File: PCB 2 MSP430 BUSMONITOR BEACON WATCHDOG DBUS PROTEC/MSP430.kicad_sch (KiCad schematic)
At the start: 1 part

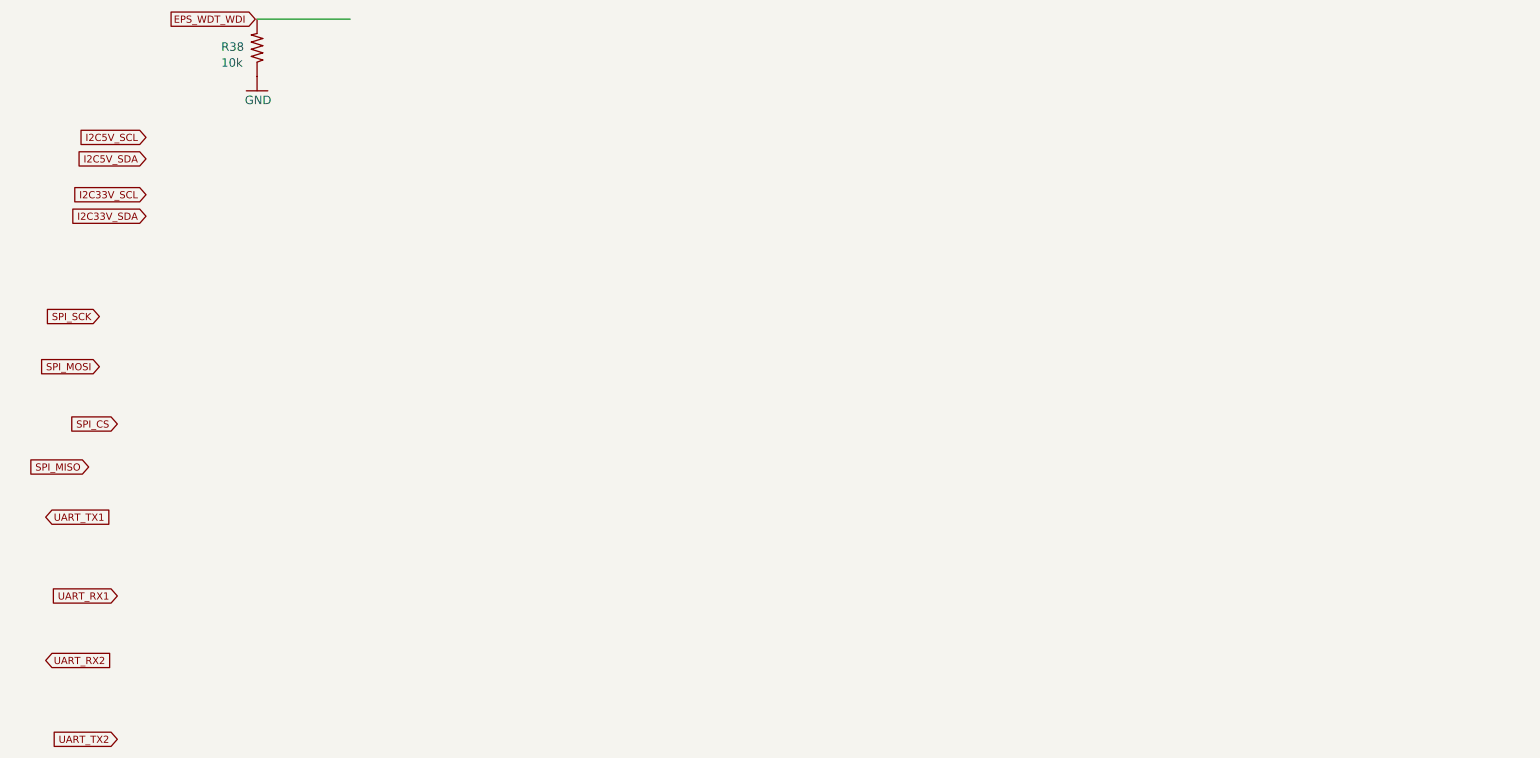
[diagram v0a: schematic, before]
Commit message: Changes
Added bucks from old work
and copied SPV
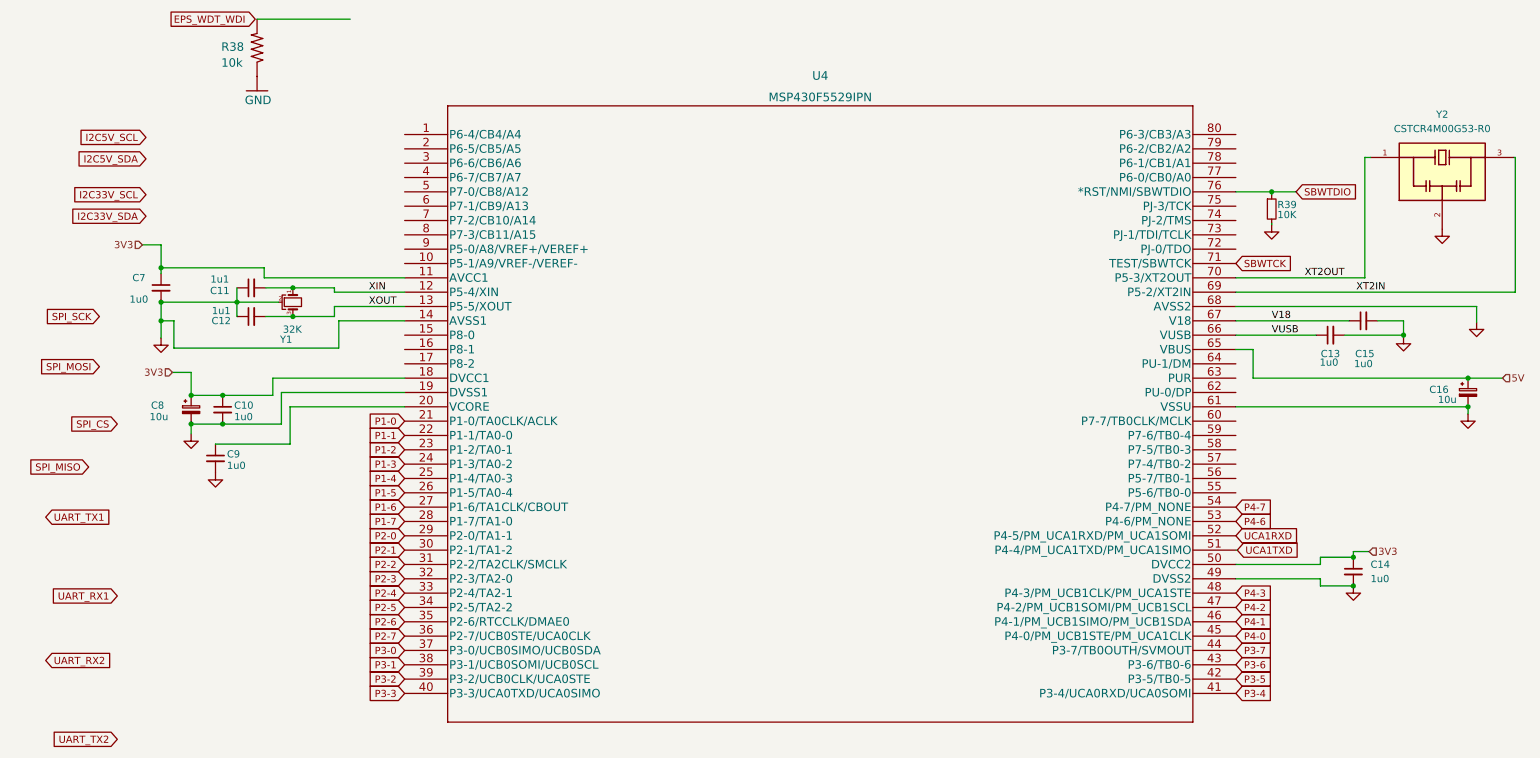
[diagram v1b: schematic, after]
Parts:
- added C10, C14, C7, C9: 1u0, Capacitor_SMD:C_0603_1608Metric, symbol Device:C_Small
- added C11, C12: 1u1, Capacitor_SMD:C_0603_1608Metric, symbol Device:C_Small
- added C13, C15: 1u0, Capacitor_SMD:C_0402_1005Metric_Pad0.74x0.62mm_HandSolder, symbol Device:C_Small
- added C16: 10u, Capacitor_SMD:CP_Elec_4x3.9, symbol Device:C_Polarized_Small
- added C8: 10u, Capacitor_SMD:CP_Elec_3x5.3, symbol Device:C_Polarized_Small
- added R39: 10K, Resistor_SMD:R_0603_1608Metric, symbol Device:R_Small
- added U4: MSP430F5529IPN, footprintMSP:MSP430F5529IPN, symbol 2023-03-28_15-31-46:MSP430F5529IPN
- added Y1: 32K, Crystal:Crystal_AT310_D3.0mm_L10.0mm_Horizontal_1EP_style1, symbol Device:Crystal_GND2_Small
- added Y2: CSTCR4M00G53-R0, CSTCR4M00G53-R0:OSC_CSTCR4M00G53-R0, symbol CSTCR4M00G53-R0:CSTCR4M00G53-R0
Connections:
- net GND: now also C10.2, C11.1, C12.1, C13.2, C14.2, C15.2, C16.2, C7.2, C8.2, C9.2, R39.2, U4.14 (AVSS1), U4.19 (DVSS1), U4.49 (DVSS2), U4.61 (VSSU), U4.68 (AVSS2), Y1.2, Y2.2
- new net: C9.1, U4.20 (VCORE)
- new net 3V3: C10.1, C14.1, C7.1, C8.1, U4.11 (AVCC1), U4.18 (DVCC1), U4.50 (DVCC2)
- new net 5V: C16.1, U4.65 (VBUS)
- new net P1-0: U4.21 (P1-0/TA0CLK/ACLK)
- new net P1-1: U4.22 (P1-1/TA0-0)
- new net P1-2: U4.23 (P1-2/TA0-1)
- new net P1-3: U4.24 (P1-3/TA0-2)
- new net P1-4: U4.25 (P1-4/TA0-3)
- new net P1-5: U4.26 (P1-5/TA0-4)
- new net P1-6: U4.27 (P1-6/TA1CLK/CBOUT)
- new net P1-7: U4.28 (P1-7/TA1-0)
- new net P2-0: U4.29 (P2-0/TA1-1)
- new net P2-1: U4.30 (P2-1/TA1-2)
- new net P2-2: U4.31 (P2-2/TA2CLK/SMCLK)
- new net P2-3: U4.32 (P2-3/TA2-0)
- new net P2-4: U4.33 (P2-4/TA2-1)
- new net P2-5: U4.34 (P2-5/TA2-2)
- new net P2-6: U4.35 (P2-6/RTCCLK/DMAE0)
- new net P2-7: U4.36 (P2-7/UCB0STE/UCA0CLK)
- new net P3-0: U4.37 (P3-0/UCB0SIMO/UCB0SDA)
- new net P3-1: U4.38 (P3-1/UCB0SOMI/UCB0SCL)
- new net P3-2: U4.39 (P3-2/UCB0CLK/UCA0STE)
- new net P3-3: U4.40 (P3-3/UCA0TXD/UCA0SIMO)
- new net P3-4: U4.41 (P3-4/UCA0RXD/UCA0SOMI)
- new net P3-5: U4.42 (P3-5/TB0-5)
- new net P3-6: U4.43 (P3-6/TB0-6)
- new net P3-7: U4.44 (P3-7/TB0OUTH/SVMOUT)
- new net P4-0: U4.45 (P4-0/PM_UCB1STE/PM_UCA1CLK)
- new net P4-1: U4.46 (P4-1/PM_UCB1SIMO/PM_UCB1SDA)
- new net P4-2: U4.47 (P4-2/PM_UCB1SOMI/PM_UCB1SCL)
- new net P4-3: U4.48 (P4-3/PM_UCB1CLK/PM_UCA1STE)
- new net P4-6: U4.53 (P4-6/PM_NONE)
- new net P4-7: U4.54 (P4-7/PM_NONE)
- new net SBWTCK: U4.71 (TEST/SBWTCK)
- new net SBWTDIO: R39.1, U4.76 (*RST/NMI/SBWTDIO)
- new net UCA1RXD: U4.52 (P4-5/PM_UCA1RXD/PM_UCA1SOMI)
- new net UCA1TXD: U4.51 (P4-4/PM_UCA1TXD/PM_UCA1SIMO)
- new net V18: C15.1, U4.67 (V18)
- new net VUSB: C13.1, U4.66 (VUSB)
- new net XIN: C11.2, U4.12 (P5-4/XIN), Y1.1
- new net XOUT: C12.2, U4.13 (P5-5/XOUT), Y1.3
- new net XT2IN: U4.69 (P5-2/XT2IN), Y2.3
- new net XT2OUT: U4.70 (P5-3/XT2OUT), Y2.1

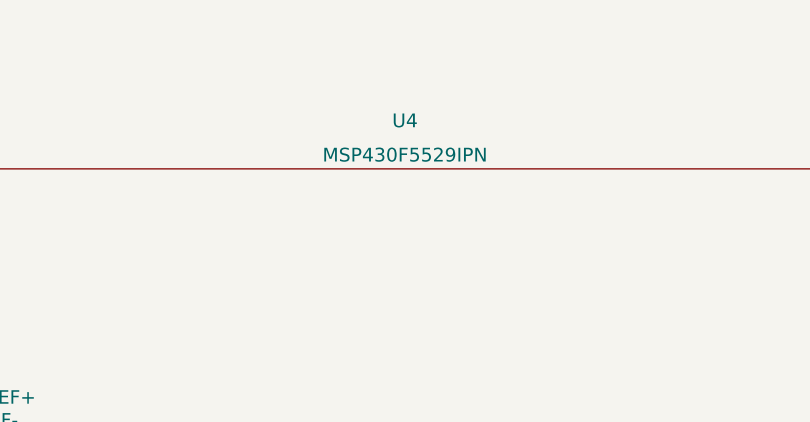
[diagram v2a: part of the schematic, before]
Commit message: Redisgnated components in PCB2 to make more sense
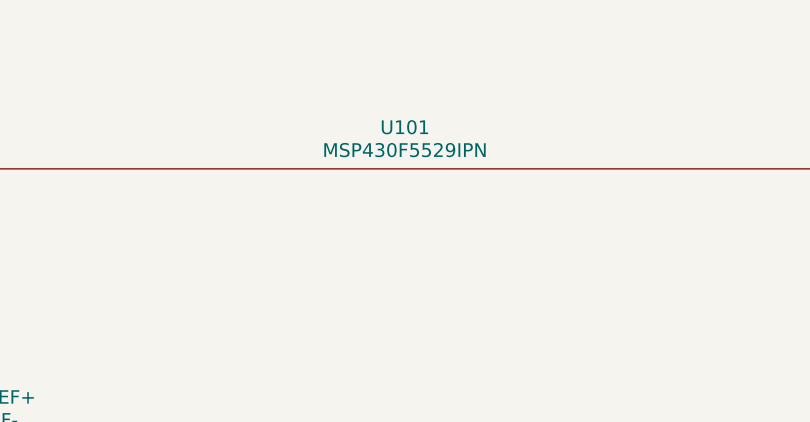
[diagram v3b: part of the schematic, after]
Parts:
- renumbered U4 to U101
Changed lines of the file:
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@@
 		(dnp no)
 		(fields_autoplaced yes)
-		(property "Reference" "U4"
-			(at 158.242 47.498 0)
+		(property "Reference" "U101"
+			(at 158.242 48.26 0)
 			(effects
 				(font
@@
 		)
 		(property "Value" "MSP430F5529IPN"
-			(at 158.242 51.308 0)
+			(at 158.242 50.8 0)
 			(effects
 				(font
@@
 			(project "PCB 2 MSP430 BUSMONITOR BEACON WATCHDOG DBUS PROTEC"
 				(path "/04a95c0c-1f2d-49e4-8823-3428ac263eb8/29b19617-a0de-4dbb-a0d0-bdecf21ca8e4"
-					(reference "U4")
+					(reference "U101")
 					(unit 1)
 				)
